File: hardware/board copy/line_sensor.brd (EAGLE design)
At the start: 104 x 52.7 mm, 68 parts, among them IC1 STM32F051K4U, J1 XF2L-0535-1, J5 XF2L-0535-1, Q1 BSS123

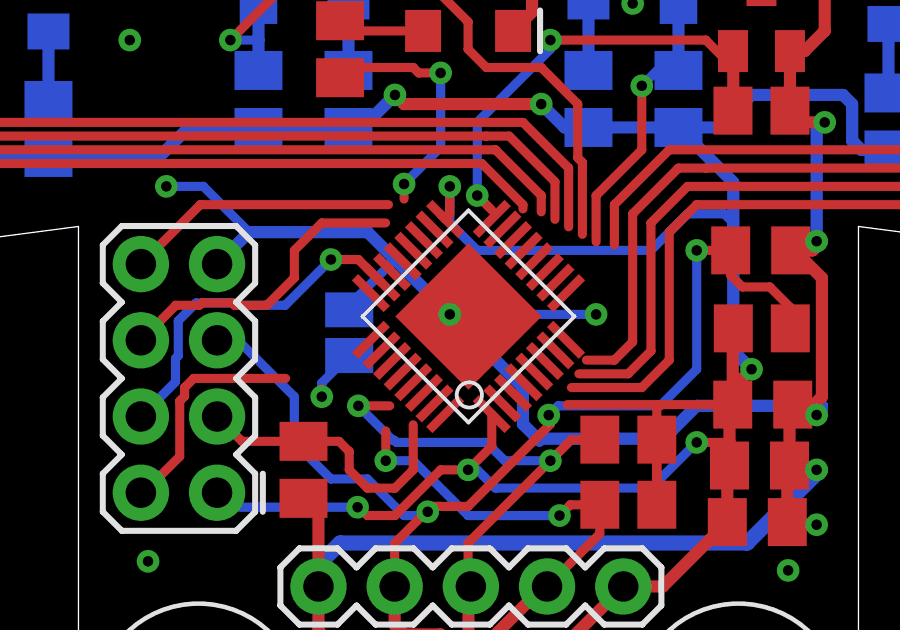
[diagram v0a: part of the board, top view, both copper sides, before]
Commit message: i2c slave - bugs on stm32f0
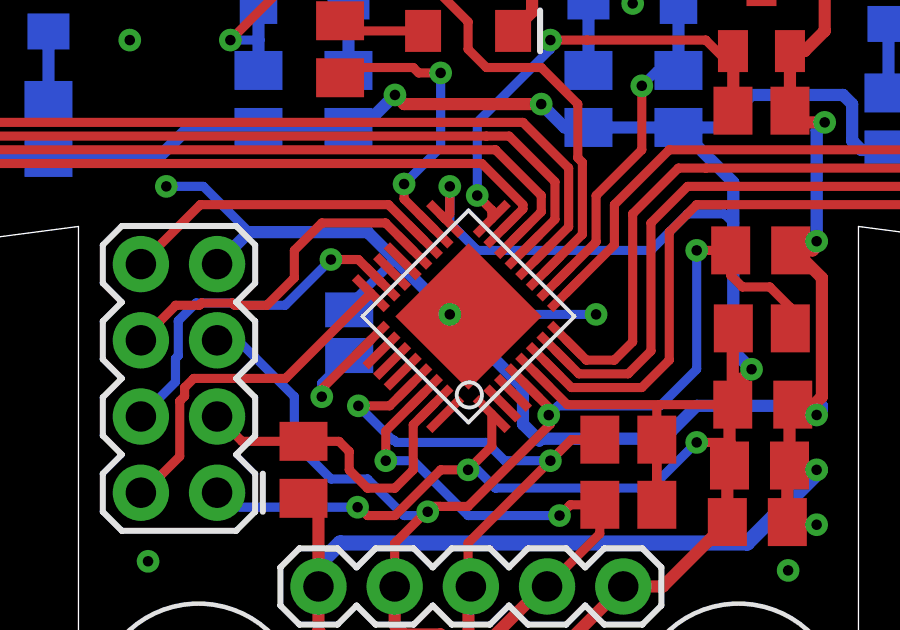
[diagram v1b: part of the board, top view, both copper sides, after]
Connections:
- removed net VDDA: IC1.5
- net +3V3: now also IC1.5
- net ADC0: now also IC1.6
- net ADC1: now also IC1.7
- net ADC2: now also IC1.8
- net ADC3: now also IC1.9
- net ADC4: now also IC1.10
- net ADC5: now also IC1.11
- net ADC6: now also IC1.12
- net ADC7: now also IC1.13
- net ADC8: now also IC1.14
- net ADC9: now also IC1.15
- net ADR: now also IC1.25
- net BOOT: now also IC1.31
- net LED: now also IC1.18
- net LED_CONTROL: now also IC1.16
- net RESET: now also IC1.4
- net SCL: now also IC1.30
- net SDA: now also IC1.29
- net SWCLK: now also IC1.24
- net SWDIO: now also IC1.23
- net UART_RX: now also IC1.20
- net UART_TX: now also IC1.19
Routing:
- net SWCLK: track 7.65 -> 11.7 mm
- net ADR: track 2.01 -> 4.32 mm
- net ADC3: track 21.2 -> 23.5 mm
- net ADC4: track 9.67 -> 11.6 mm
- net SCL: track 22.3 -> 24.1 mm
- net ADC5: track 22.5 -> 24.3 mm
- net UART_TX: track 9.07 -> 10.7 mm
- net ADC6: track 28.6 -> 30.3 mm
- net +3V3: track 182.6 -> 184.2 mm
- net ADC7: track 36.6 -> 38.1 mm
- net LED: track 8.28 -> 9.71 mm
- net ADC8: track 46.1 -> 47.4 mm
- net UART_RX: track 10.4 -> 11.7 mm
- net RESET: track 44.6 -> 45.8 mm
- net ADC0: track 54.7 -> 56.0 mm
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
